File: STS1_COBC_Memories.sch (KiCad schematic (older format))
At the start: 7 parts

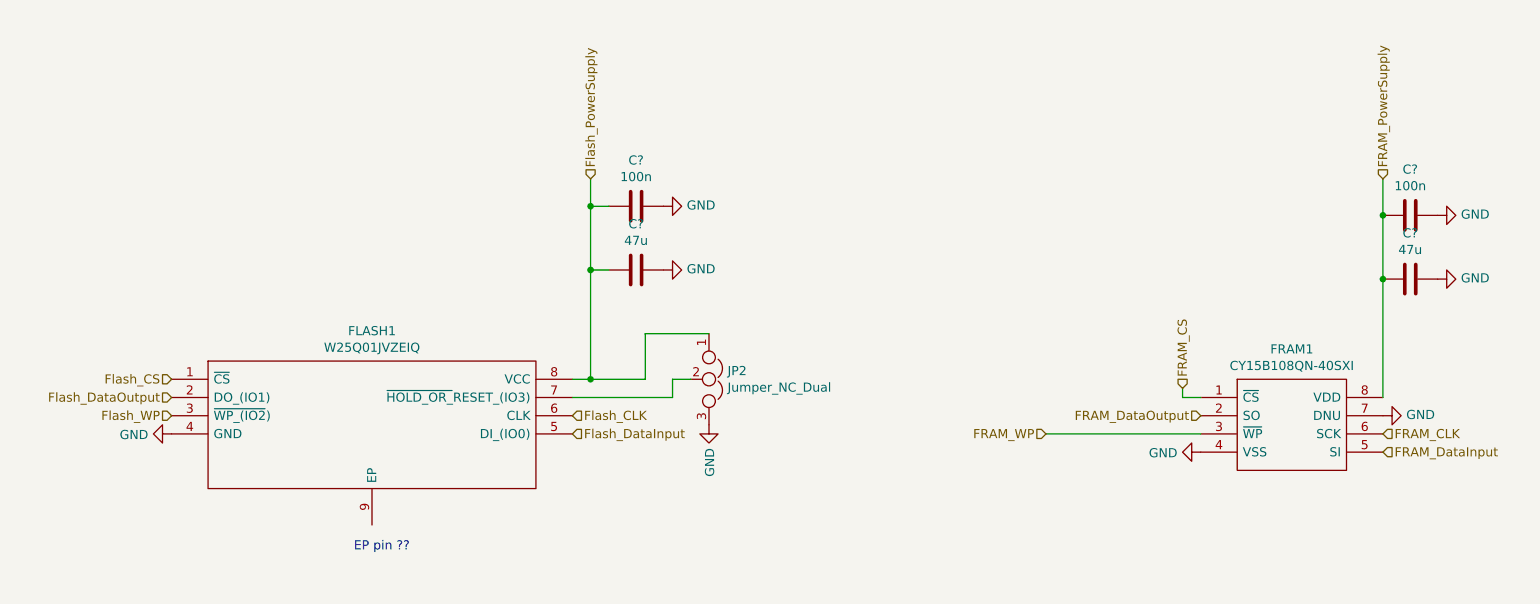
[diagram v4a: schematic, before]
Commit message: Issues removed + further layout development
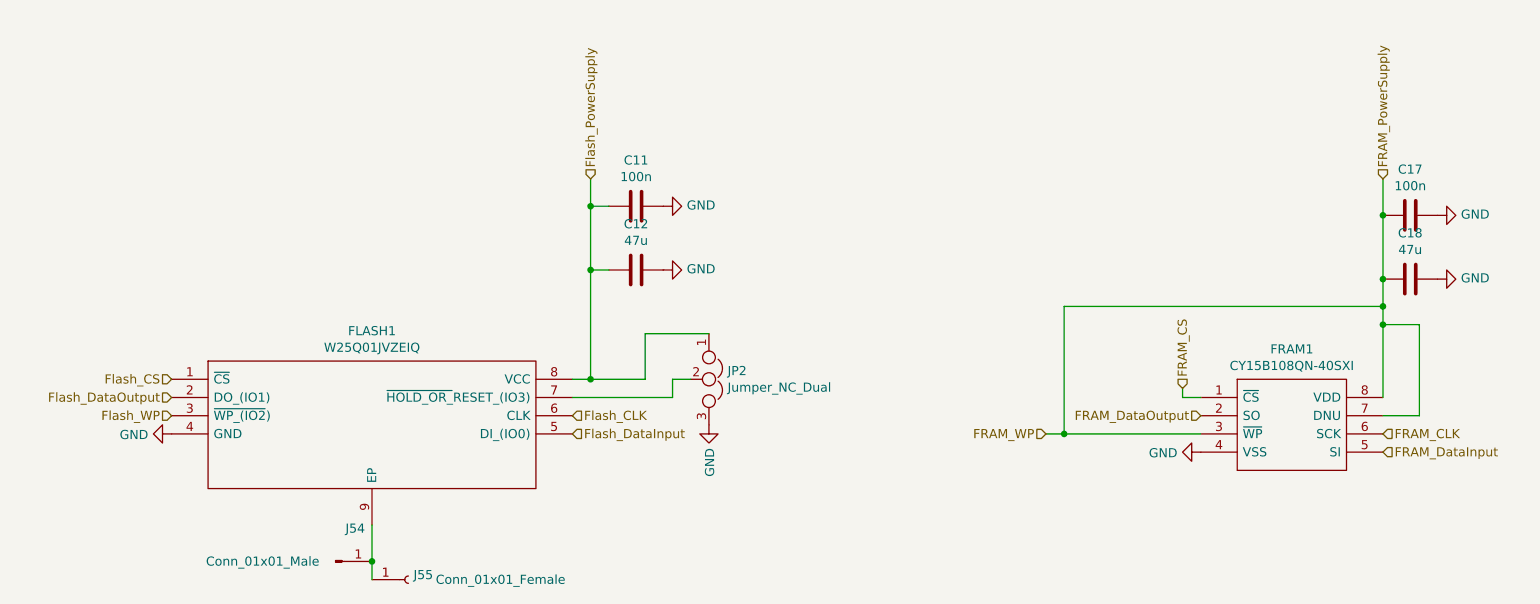
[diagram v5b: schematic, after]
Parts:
- added J54: Conn_01x01_Male, symbol Connector:Conn_01x01_Male
- added J55: Conn_01x01_Female, symbol Connector:Conn_01x01_Female
- C11, C12, C17, C18: renamed from C?; footprint (none) -> Capacitor_SMD:C_0805_2012Metric
- JP2: footprint (none) -> Connector_PinHeader_2.54mm:PinHeader_1x03_P2.54mm_Vertical
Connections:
- net FRAM_WP is gone; now on net FRAM_PowerSupply: FRAM1.3 (~WP)
- net FRAM_PowerSupply: now also FRAM1.7 (DNU)
- net GND: no longer FRAM1.7 (DNU)
- net at FLASH1.9 (EP): now also J54.1 (Pin_1), J55.1 (Pin_1)
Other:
- note removed: "EP pin ??\n"
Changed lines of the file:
@@
 $EndComp
 Wire Wire Line
-	6900 3100 7750 3100
+	6900 3100 7000 3100
 Text HLabel 7650 2850 1    50   Input ~ 0
 FRAM_CS
@@
 Text HLabel 2100 3000 0    50   Input ~ 0
 Flash_WP
-Text Notes 3100 3750 0    50   ~ 0
-EP pin ??\n
 Wire Wire Line
 	4300 2800 4400 2800
@@
 F 0 "JP2" V 5004 2902 50  0000 L CNN
 F 1 "Jumper_NC_Dual" V 5095 2902 50  0000 L CNN
-F 2 "" H 5050 2800 50  0001 C CNN
+F 2 "Connector_PinHeader_2.54mm:PinHeader_1x03_P2.54mm_Vertical" H 5050 2800 50  0001 C CNN
 F 3 "~" H 5050 2800 50  0001 C CNN
 	1    5050 2800
@@
 FRAM_WP
 $Comp
-L power:GND #PWR0141
-U 1 1 616C77F0
-P 8750 3000
-F 0 "#PWR0141" H 8750 2750 50  0001 C CNN
-F 1 "GND" V 8755 2872 50  0000 R CNN
-F 2 "" H 8750 3000 50  0001 C CNN
-F 3 "" H 8750 3000 50  0001 C CNN
-	1    8750 3000
-	0    -1   -1   0
-$EndComp
-$Comp
-L Device:C C?
+L Device:C C11
 U 1 1 61691DC4
 P 4650 1850
-F 0 "C?" V 4398 1850 50  0000 C CNN
+F 0 "C11" V 4398 1850 50  0000 C CNN
 F 1 "100n" V 4489 1850 50  0000 C CNN
-F 2 "" H 4688 1700 50  0001 C CNN
+F 2 "Capacitor_SMD:C_0805_2012Metric" H 4688 1700 50  0001 C CNN
 F 3 "~" H 4650 1850 50  0001 C CNN
 	1    4650 1850
@@
 $EndComp
 $Comp
-L Device:C C?
+L Device:C C12
 U 1 1 61692327
 P 4650 2200
-F 0 "C?" V 4398 2200 50  0000 C CNN
+F 0 "C12" V 4398 2200 50  0000 C CNN
 F 1 "47u" V 4489 2200 50  0000 C CNN
-F 2 "" H 4688 2050 50  0001 C CNN
+F 2 "Capacitor_SMD:C_0805_2012Metric" H 4688 2050 50  0001 C CNN
 F 3 "~" H 4650 2200 50  0001 C CNN
 	1    4650 2200
@@
 $EndComp
 $Comp
-L power:GND #PWR?
+L power:GND #PWR0106
 U 1 1 61692683
 P 4800 2200
-F 0 "#PWR?" H 4800 1950 50  0001 C CNN
+F 0 "#PWR0106" H 4800 1950 50  0001 C CNN
 F 1 "GND" V 4805 2072 50  0000 R CNN
 F 2 "" H 4800 2200 50  0001 C CNN
@@
 $EndComp
 $Comp
-L power:GND #PWR?
+L power:GND #PWR0107
 U 1 1 61692ABE
 P 4800 1850
-F 0 "#PWR?" H 4800 1600 50  0001 C CNN
+F 0 "#PWR0107" H 4800 1600 50  0001 C CNN
 F 1 "GND" V 4805 1722 50  0000 R CNN
 F 2 "" H 4800 1850 50  0001 C CNN
@@
 	4400 1850 4400 2200
 $Comp
-L Device:C C?
+L Device:C C17
 U 1 1 61694B9B
 P 8900 1900
-F 0 "C?" V 8648 1900 50  0000 C CNN
+F 0 "C17" V 8648 1900 50  0000 C CNN
 F 1 "100n" V 8739 1900 50  0000 C CNN
-F 2 "" H 8938 1750 50  0001 C CNN
+F 2 "Capacitor_SMD:C_0805_2012Metric" H 8938 1750 50  0001 C CNN
 F 3 "~" H 8900 1900 50  0001 C CNN
 	1    8900 1900
@@
 $EndComp
 $Comp
-L Device:C C?
+L Device:C C18
 U 1 1 61694BA1
 P 8900 2250
-F 0 "C?" V 8648 2250 50  0000 C CNN
+F 0 "C18" V 8648 2250 50  0000 C CNN
 F 1 "47u" V 8739 2250 50  0000 C CNN
-F 2 "" H 8938 2100 50  0001 C CNN
+F 2 "Capacitor_SMD:C_0805_2012Metric" H 8938 2100 50  0001 C CNN
 F 3 "~" H 8900 2250 50  0001 C CNN
 	1    8900 2250
@@
 $EndComp
 $Comp
-L power:GND #PWR?
+L power:GND #PWR0108
 U 1 1 61694BA7
 P 9050 2250
-F 0 "#PWR?" H 9050 2000 50  0001 C CNN
+F 0 "#PWR0108" H 9050 2000 50  0001 C CNN
 F 1 "GND" V 9055 2122 50  0000 R CNN
 F 2 "" H 9050 2250 50  0001 C CNN
@@
 $EndComp
 $Comp
-L power:GND #PWR?
+L power:GND #PWR0109
 U 1 1 61694BAD
 P 9050 1900
-F 0 "#PWR?" H 9050 1650 50  0001 C CNN
+F 0 "#PWR0109" H 9050 1650 50  0001 C CNN
 F 1 "GND" V 9055 1772 50  0000 R CNN
 F 2 "" H 9050 1900 50  0001 C CNN
@@
 Connection ~ 8750 2250
 Wire Wire Line
-	8750 2250 8750 2900
+	8750 2250 8750 2400
+Wire Wire Line
+	7000 3100 7000 2400
+Wire Wire Line
+	7000 2400 8750 2400
+Connection ~ 7000 3100
+Wire Wire Line
+	7000 3100 7750 3100
+Connection ~ 8750 2400
+Wire Wire Line
+	8750 2400 8750 2500
+Wire Wire Line
+	8750 3000 8950 3000
+Wire Wire Line
+	8950 3000 8950 2500
+Wire Wire Line
+	8950 2500 8750 2500
+Connection ~ 8750 2500
+Wire Wire Line
+	8750 2500 8750 2900
+$Comp
+L Connector:Conn_01x01_Male J54
+U 1 1 6182DF07
+P 3000 3800
+F 0 "J54" H 3108 3981 50  0000 C CNN
+F 1 "Conn_01x01_Male" H 2600 3800 50  0000 C CNN
+F 2 "" H 3000 3800 50  0001 C CNN
+F 3 "~" H 3000 3800 50  0001 C CNN
+	1    3000 3800
+	1    0    0    -1
+$EndComp
+$Comp
+L Connector:Conn_01x01_Female J55
+U 1 1 6182EA34
+P 3400 3900
+F 0 "J55" H 3428 3926 50  0000 L CNN
+F 1 "Conn_01x01_Female" H 3550 3900 50  0000 L CNN
+F 2 "" H 3400 3900 50  0001 C CNN
+F 3 "~" H 3400 3900 50  0001 C CNN
+	1    3400 3900
+	1    0    0    -1
+$EndComp
+Wire Wire Line
+	3200 3600 3200 3800
+Connection ~ 3200 3800
+Wire Wire Line
+	3200 3800 3200 3900
 $EndSCHEMATC

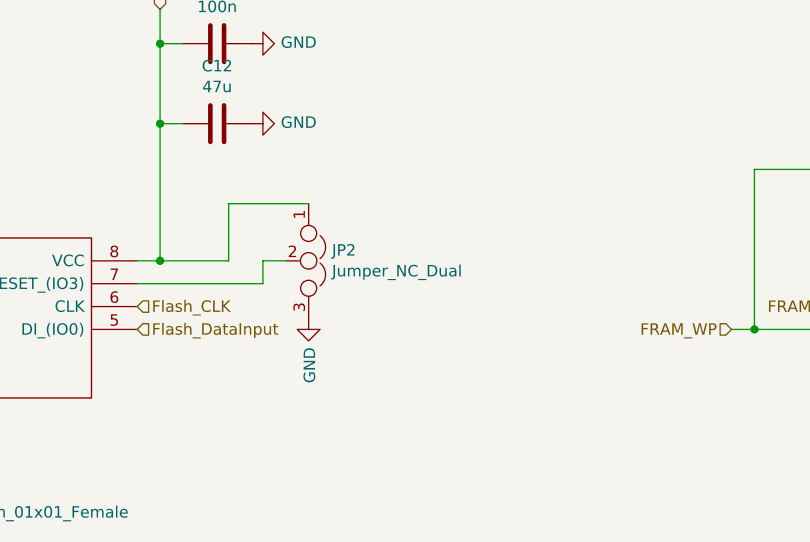
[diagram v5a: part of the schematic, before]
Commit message: component layout finished -> now wiring
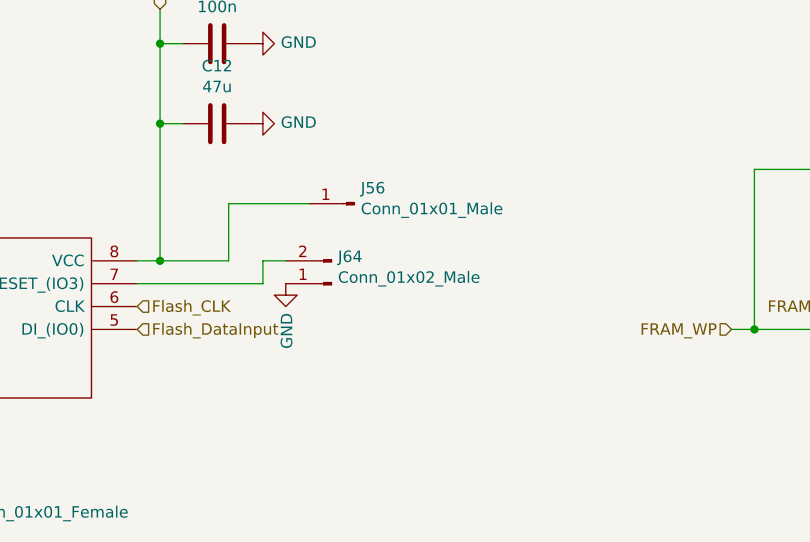
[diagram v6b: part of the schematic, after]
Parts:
- removed JP2: Jumper_NC_Dual, Connector_PinHeader_2.54mm:PinHeader_1x03_P2.54mm_Vertical, symbol Device:Jumper_NC_Dual
- added J56: Conn_01x01_Male, Connector_PinHeader_2.54mm:PinHeader_1x01_P2.54mm_Vertical, symbol Connector:Conn_01x01_Male
- added J64: Conn_01x02_Male, Connector_PinHeader_2.54mm:PinHeader_1x02_P2.54mm_Vertical, symbol Connector:Conn_01x02_Male
- J54, J55: footprint (none) -> Connector_PinHeader_2.54mm:PinHeader_1x01_P2.54mm_Vertical
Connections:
- net Flash_PowerSupply: now also J56.1 (Pin_1)
- net GND: now also J64.1 (Pin_1)
- net at FLASH1.7 (~HOLD_OR_~RESET_(IO3)): now also J64.2 (Pin_2)
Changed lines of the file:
@@
 	4300 2800 4400 2800
-$Comp
-L Device:Jumper_NC_Dual JP2
-U 1 1 616C1C39
-P 5050 2800
-F 0 "JP2" V 5004 2902 50  0000 L CNN
-F 1 "Jumper_NC_Dual" V 5095 2902 50  0000 L CNN
-F 2 "Connector_PinHeader_2.54mm:PinHeader_1x03_P2.54mm_Vertical" H 5050 2800 50  0001 C CNN
-F 3 "~" H 5050 2800 50  0001 C CNN
-	1    5050 2800
-	0    1    1    0
-$EndComp
 $Comp
 L power:GND #PWR0123
 U 1 1 616C2B2C
-P 5050 3050
-F 0 "#PWR0123" H 5050 2800 50  0001 C CNN
-F 1 "GND" V 5055 2922 50  0000 R CNN
-F 2 "" H 5050 3050 50  0001 C CNN
-F 3 "" H 5050 3050 50  0001 C CNN
-	1    5050 3050
+P 4950 2900
+F 0 "#PWR0123" H 4950 2650 50  0001 C CNN
+F 1 "GND" V 4955 2772 50  0000 R CNN
+F 2 "" H 4950 2900 50  0001 C CNN
+F 3 "" H 4950 2900 50  0001 C CNN
+	1    4950 2900
 	1    0    0    -1
 $EndComp
@@
 F 0 "J54" H 3108 3981 50  0000 C CNN
 F 1 "Conn_01x01_Male" H 2600 3800 50  0000 C CNN
-F 2 "" H 3000 3800 50  0001 C CNN
+F 2 "Connector_PinHeader_2.54mm:PinHeader_1x01_P2.54mm_Vertical" H 3000 3800 50  0001 C CNN
 F 3 "~" H 3000 3800 50  0001 C CNN
 	1    3000 3800
@@
 F 0 "J55" H 3428 3926 50  0000 L CNN
 F 1 "Conn_01x01_Female" H 3550 3900 50  0000 L CNN
-F 2 "" H 3400 3900 50  0001 C CNN
+F 2 "Connector_PinHeader_2.54mm:PinHeader_1x01_P2.54mm_Vertical" H 3400 3900 50  0001 C CNN
 F 3 "~" H 3400 3900 50  0001 C CNN
 	1    3400 3900
@@
 Wire Wire Line
 	3200 3800 3200 3900
+$Comp
+L Connector:Conn_01x01_Male J56
+U 1 1 618B70AC
+P 5250 2550
+F 0 "J56" H 5222 2482 50  0000 R CNN
+F 1 "Conn_01x01_Male" H 5222 2573 50  0000 R CNN
+F 2 "Connector_PinHeader_2.54mm:PinHeader_1x01_P2.54mm_Vertical" H 5250 2550 50  0001 C CNN
+F 3 "~" H 5250 2550 50  0001 C CNN
+	1    5250 2550
+	-1   0    0    1
+$EndComp
+$Comp
+L Connector:Conn_01x02_Male J64
+U 1 1 618CCC73
+P 5150 2900
+F 0 "J64" H 5122 2782 50  0000 R CNN
+F 1 "Conn_01x02_Male" H 5122 2873 50  0000 R CNN
+F 2 "Connector_PinHeader_2.54mm:PinHeader_1x02_P2.54mm_Vertical" H 5150 2900 50  0001 C CNN
+F 3 "~" H 5150 2900 50  0001 C CNN
+	1    5150 2900
+	-1   0    0    1
+$EndComp
 $EndSCHEMATC

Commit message: final version1
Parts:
- removed J56: Conn_01x01_Male, Connector_PinHeader_2.54mm:PinHeader_1x01_P2.54mm_Vertical, symbol Connector:Conn_01x01_Male
- removed J64: Conn_01x02_Male, Connector_PinHeader_2.54mm:PinHeader_1x02_P2.54mm_Vertical, symbol Connector:Conn_01x02_Male
- added J2: Conn_01x03_Male, STS1library:PinHeader_1x03_P2.54mm_Vertical_umdieEcke, symbol Connector:Conn_01x03_Male
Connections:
- net Flash_PowerSupply: now also J2.3 (Pin_3)
- net GND: now also J2.1 (Pin_1)
- net at FLASH1.7 (~HOLD_OR_~RESET_(IO3)): now also J2.2 (Pin_2)
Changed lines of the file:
@@
 $Descr A4 11693 8268
 encoding utf-8
-Sheet 2 5
+Sheet 2 6
 Title ""
 Date ""
@@
 P 2100 3100
 F 0 "#PWR0139" H 2100 2850 50  0001 C CNN
-F 1 "GND" V 2105 2972 50  0000 R CNN
+F 1 "GND" H 2105 2972 50  0000 R CNN
 F 2 "" H 2100 3100 50  0001 C CNN
 F 3 "" H 2100 3100 50  0001 C CNN
 	1    2100 3100
-	0    1    1    0
+	1    0    0    -1
 $EndComp
 $Comp
@@
 P 7750 3200
 F 0 "#PWR0140" H 7750 2950 50  0001 C CNN
-F 1 "GND" V 7755 3072 50  0000 R CNN
+F 1 "GND" H 7750 3050 50  0000 R CNN
 F 2 "" H 7750 3200 50  0001 C CNN
 F 3 "" H 7750 3200 50  0001 C CNN
 	1    7750 3200
-	0    1    1    0
+	1    0    0    -1
 $EndComp
 Wire Wire Line
@@
 	4300 2900 4850 2900
 Wire Wire Line
-	5050 2550 4700 2550
-Wire Wire Line
 	4700 2550 4700 2800
 Wire Wire Line
@@
 P 4800 2200
 F 0 "#PWR0106" H 4800 1950 50  0001 C CNN
-F 1 "GND" V 4805 2072 50  0000 R CNN
+F 1 "GND" H 4950 2050 50  0000 R CNN
 F 2 "" H 4800 2200 50  0001 C CNN
 F 3 "" H 4800 2200 50  0001 C CNN
 	1    4800 2200
-	0    -1   -1   0
+	1    0    0    -1
 $EndComp
 $Comp
@@
 P 4800 1850
 F 0 "#PWR0107" H 4800 1600 50  0001 C CNN
-F 1 "GND" V 4805 1722 50  0000 R CNN
+F 1 "GND" H 4950 1700 50  0000 R CNN
 F 2 "" H 4800 1850 50  0001 C CNN
 F 3 "" H 4800 1850 50  0001 C CNN
 	1    4800 1850
-	0    -1   -1   0
+	1    0    0    -1
 $EndComp
 Wire Wire Line
@@
 P 9050 2250
 F 0 "#PWR0108" H 9050 2000 50  0001 C CNN
-F 1 "GND" V 9055 2122 50  0000 R CNN
+F 1 "GND" H 9200 2100 50  0000 R CNN
 F 2 "" H 9050 2250 50  0001 C CNN
 F 3 "" H 9050 2250 50  0001 C CNN
 	1    9050 2250
-	0    -1   -1   0
+	1    0    0    -1
 $EndComp
 $Comp
@@
 P 9050 1900
 F 0 "#PWR0109" H 9050 1650 50  0001 C CNN
-F 1 "GND" V 9055 1772 50  0000 R CNN
+F 1 "GND" H 9200 1750 50  0000 R CNN
 F 2 "" H 9050 1900 50  0001 C CNN
 F 3 "" H 9050 1900 50  0001 C CNN
 	1    9050 1900
-	0    -1   -1   0
+	1    0    0    -1
 $EndComp
 Wire Wire Line
@@
 	3200 3800 3200 3900
 $Comp
-L Connector:Conn_01x01_Male J56
-U 1 1 618B70AC
-P 5250 2550
-F 0 "J56" H 5222 2482 50  0000 R CNN
-F 1 "Conn_01x01_Male" H 5222 2573 50  0000 R CNN
-F 2 "Connector_PinHeader_2.54mm:PinHeader_1x01_P2.54mm_Vertical" H 5250 2550 50  0001 C CNN
-F 3 "~" H 5250 2550 50  0001 C CNN
-	1    5250 2550
+L Connector:Conn_01x03_Male J2
+U 1 1 61B42D81
+P 5150 2800
+F 0 "J2" H 5122 2732 50  0000 R CNN
+F 1 "Conn_01x03_Male" H 5122 2823 50  0000 R CNN
+F 2 "STS1library:PinHeader_1x03_P2.54mm_Vertical_umdieEcke" H 5150 2800 50  0001 C CNN
+F 3 "~" H 5150 2800 50  0001 C CNN
+	1    5150 2800
 	-1   0    0    1
 $EndComp
-$Comp
-L Connector:Conn_01x02_Male J64
-U 1 1 618CCC73
-P 5150 2900
-F 0 "J64" H 5122 2782 50  0000 R CNN
-F 1 "Conn_01x02_Male" H 5122 2873 50  0000 R CNN
-F 2 "Connector_PinHeader_2.54mm:PinHeader_1x02_P2.54mm_Vertical" H 5150 2900 50  0001 C CNN
-F 3 "~" H 5150 2900 50  0001 C CNN
-	1    5150 2900
-	-1   0    0    1
-$EndComp
+Wire Wire Line
+	4950 2700 4950 2550
+Wire Wire Line
+	4950 2550 4700 2550
 $EndSCHEMATC

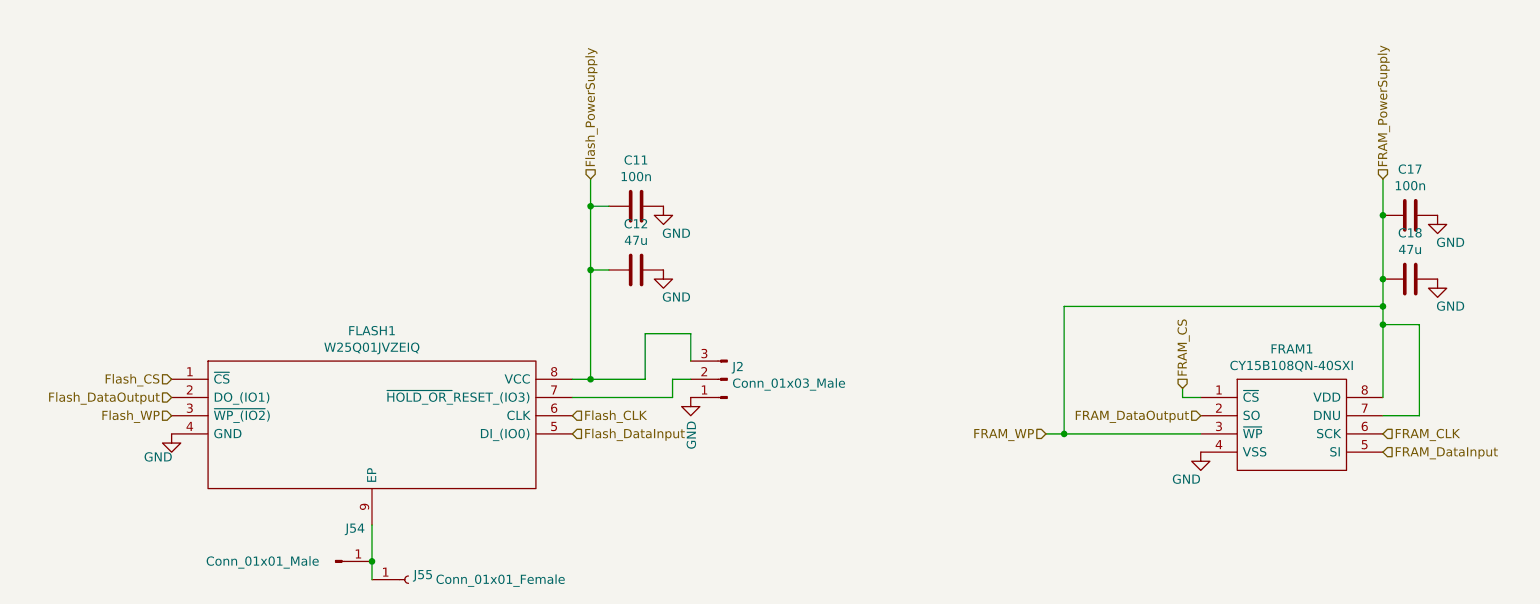
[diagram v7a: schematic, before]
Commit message: added powerplane + testpoints + some debugging
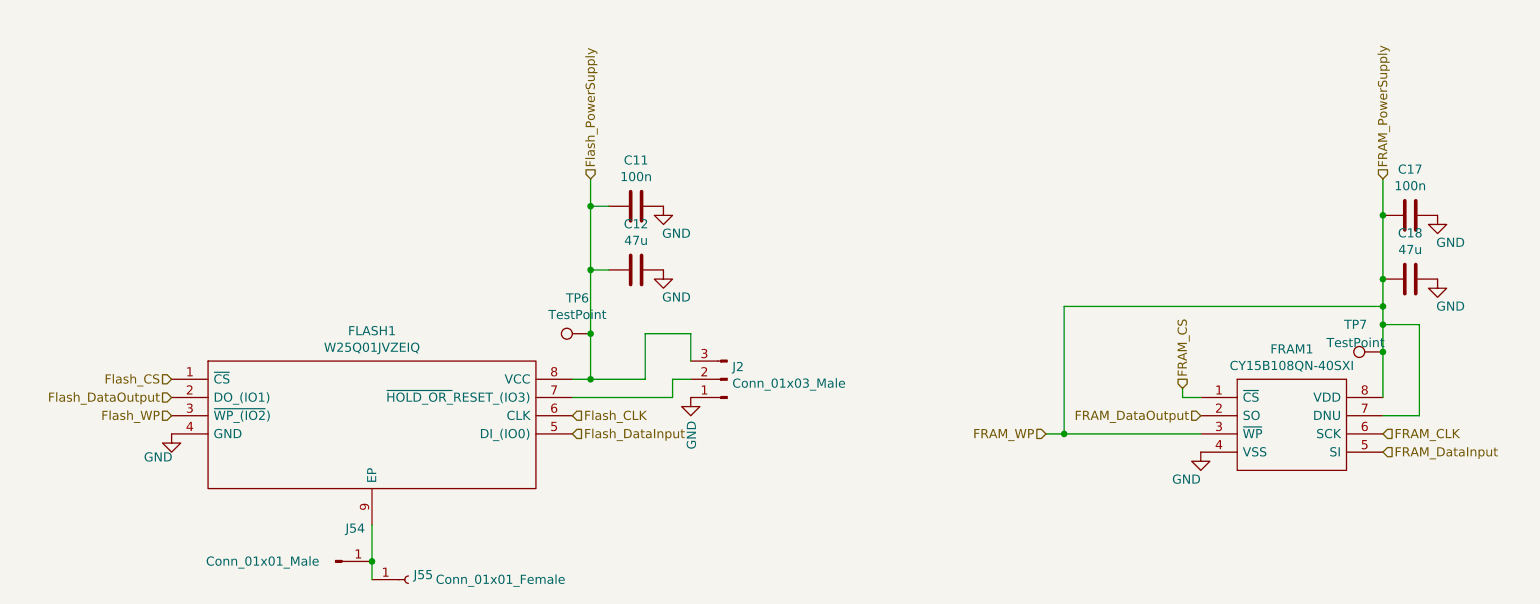
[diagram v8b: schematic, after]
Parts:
- added TP6, TP7: TestPoint, STS1library:STS1_Testpoint, symbol Connector:TestPoint
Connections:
- net FRAM_PowerSupply: now also TP7.1
- net Flash_PowerSupply: now also TP6.1
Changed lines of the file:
@@
 Connection ~ 4400 2200
 Wire Wire Line
-	4400 2200 4400 2800
+	4400 2200 4400 2550
 Wire Wire Line
 	4400 1850 4500 1850
@@
 Connection ~ 8750 2500
 Wire Wire Line
-	8750 2500 8750 2900
+	8750 2500 8750 2650
 $Comp
 L Connector:Conn_01x01_Male J54
@@
 Wire Wire Line
 	4950 2550 4700 2550
+$Comp
+L Connector:TestPoint TP6
+U 1 1 61B6C0DB
+P 4400 2550
+F 0 "TP6" V 4595 2622 50  0000 C CNN
+F 1 "TestPoint" V 4504 2622 50  0000 C CNN
+F 2 "STS1library:STS1_Testpoint" H 4600 2550 50  0001 C CNN
+F 3 "~" H 4600 2550 50  0001 C CNN
+	1    4400 2550
+	0    -1   -1   0
+$EndComp
+Connection ~ 4400 2550
+Wire Wire Line
+	4400 2550 4400 2800
+$Comp
+L Connector:TestPoint TP7
+U 1 1 61B6DAE9
+P 8750 2650
+F 0 "TP7" V 8900 2800 50  0000 C CNN
+F 1 "TestPoint" V 8800 2800 50  0000 C CNN
+F 2 "STS1library:STS1_Testpoint" H 8950 2650 50  0001 C CNN
+F 3 "~" H 8950 2650 50  0001 C CNN
+	1    8750 2650
+	0    -1   -1   0
+$EndComp
+Connection ~ 8750 2650
+Wire Wire Line
+	8750 2650 8750 2900
 $EndSCHEMATC
